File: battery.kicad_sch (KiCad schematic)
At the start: 38 parts

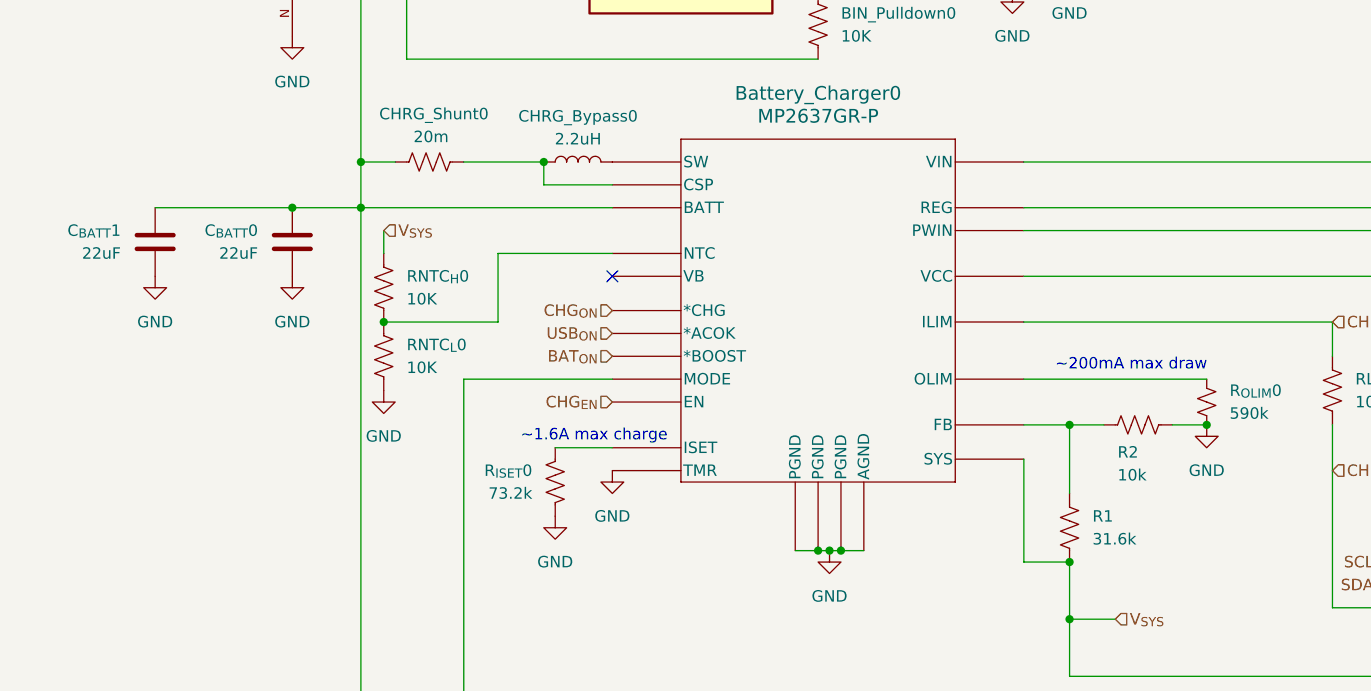
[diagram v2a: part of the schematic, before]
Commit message: Assign footprints
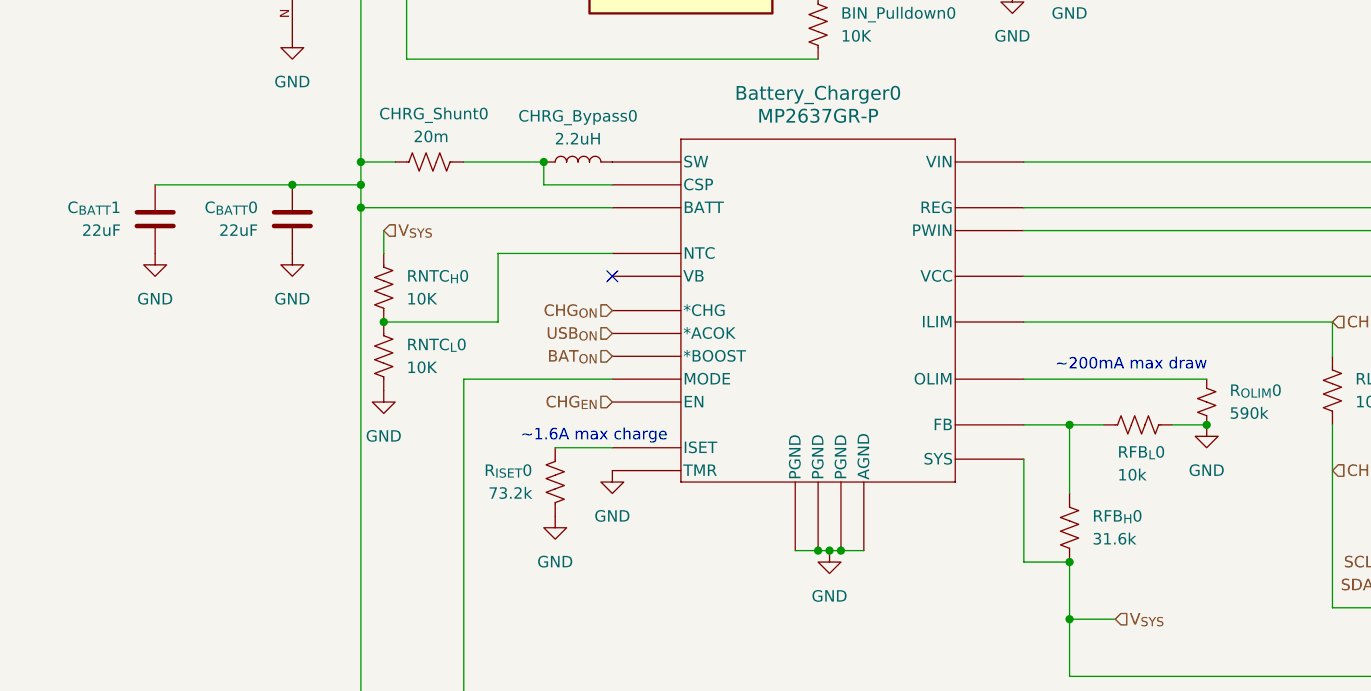
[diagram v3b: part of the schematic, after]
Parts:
- BAT0: footprint 1042:BAT_1042 -> BAT_1042
- BAT_Decouple0, CHRG_Decouple0, VDD_Decouple0: footprint (none) -> Capacitor_SMD:C_0402_1005Metric
- BAT_MIN0: footprint DMG2305UX-7:SOT91P240X110-3N_DMG2305UX-7 -> SOT91P240X110-3N_DMG2305UX-7
- BIN_Pulldown0, RLIM_{H}0, RNTC_{H}0, RNTC_{L}0, R_{ISET}0, R_{Pullup}0, R_{Store}0: footprint (none) -> Resistor_SMD:R_0402_1005Metric
- Battery_Monitor0: footprint BQ27427YZFR:IC_BQ27427YZFR -> IC_BQ27427YZFR
- CHRG_Bypass0: footprint (none) -> Inductor_SMD:L_1210_3225Metric
- CHRG_Shunt0, RREG_{H}0, R_{HIST}0: footprint (none) -> Resistor_SMD:R_0805_2012Metric
- C_{BATT}0, C_{BATT}1, C_{SYS}0, C_{SYS}1, C_{SYS}2, VBUS_Bypass0: footprint (none) -> Capacitor_SMD:C_1206_3216Metric
- RFB_{H}0: renamed from R1; footprint (none) -> Resistor_SMD:R_0402_1005Metric
- RFB_{L}0: renamed from R2; footprint (none) -> Resistor_SMD:R_0402_1005Metric
- RLIM_Decouple0: footprint (none) -> Capacitor_SMD:C_0201_0603Metric
- RLIM_{L}0: footprint MCP40D19T-104E_LT:SOT65P210X110-5N -> SOT65P210X110-5N
- RREG_{L}0, RWIN_{H}0, RWIN_{L}0, R_{Lower}0, R_{OLIM}0, R_{Upper}0: footprint (none) -> Resistor_SMD:R_0603_1608Metric
- STORE_EN0: footprint EG2208:SW_EG2208 -> SW_EG2208
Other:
- moved on the sheet: C_{BATT}0, C_{BATT}1

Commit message: Init right and left PCBs
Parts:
- renumbered BAT0 to BAT1, BAT_Decouple0 to BAT_Decouple1, BAT_EN0 to BAT_EN1, BAT_Fuse0 to BAT_Fuse1, BAT_MIN0 to BAT_MIN1, BIN_Pulldown0 to BIN_Pulldown1, Battery_Charger0 to Battery_Charger1, Battery_Monitor0 to Battery_Monitor1, CHRG_Bypass0 to CHRG_Bypass1, CHRG_Decouple0 to CHRG_Decouple1, CHRG_Shunt0 to CHRG_Shunt1, C_{BATT}0 to C_{BATT}2, C_{SYS}0 to C_{SYS}1, C_{SYS}1 to C_{SYS}2, C_{SYS}2 to C_{SYS}3, RFB_{H}0 to RFB_{H}1, RFB_{L}0 to RFB_{L}1, RLIM_Decouple0 to RLIM_Decouple1, RLIM_{H}0 to RLIM_{H}1, RLIM_{L}0 to RLIM_{L}1, RNTC_{H}0 to RNTC_{H}1, RNTC_{L}0 to RNTC_{L}1, RREG_{H}0 to RREG_{H}1, RREG_{L}0 to RREG_{L}1, RWIN_{H}0 to RWIN_{H}1, RWIN_{L}0 to RWIN_{L}1, R_{HIST}0 to R_{HIST}1, R_{ISET}0 to R_{ISET}1, R_{Lower}0 to R_{Lower}1, R_{OLIM}0 to R_{OLIM}1, R_{Pullup}0 to R_{Pullup}1, R_{Store}0 to R_{Store}1, R_{Upper}0 to R_{Upper}1, STORE_EN0 to STORE_EN1, VBAT_PASS0 to VBAT_PASS1, VBUS_Bypass0 to VBUS_Bypass1, VDD_Decouple0 to VDD_Decouple1

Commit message: Rename keyswitch diodes
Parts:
- renumbered BAT1 to BAT0, BAT_Decouple1 to BAT_Decouple0, BAT_EN1 to BAT_EN0, BAT_Fuse1 to BAT_Fuse0, BAT_MIN1 to BAT_MIN0, BIN_Pulldown1 to BIN_Pulldown0, Battery_Charger1 to Battery_Charger0, Battery_Monitor1 to Battery_Monitor0, CHRG_Bypass1 to CHRG_Bypass0, CHRG_Decouple1 to CHRG_Decouple0, CHRG_Shunt1 to CHRG_Shunt0, C_{BATT}2 to C_{BATT}0, C_{SYS}1 to C_{SYS}0, C_{SYS}2 to C_{SYS}1, C_{SYS}3 to C_{SYS}2, RFB_{H}1 to RFB_{H}0, RFB_{L}1 to RFB_{L}0, RLIM_Decouple1 to RLIM_Decouple0, RLIM_{H}1 to RLIM_{H}0, RLIM_{L}1 to RLIM_{L}0, RNTC_{H}1 to RNTC_{H}0, RNTC_{L}1 to RNTC_{L}0, RREG_{H}1 to RREG_{H}0, RREG_{L}1 to RREG_{L}0, RWIN_{H}1 to RWIN_{H}0, RWIN_{L}1 to RWIN_{L}0, R_{HIST}1 to R_{HIST}0, R_{ISET}1 to R_{ISET}0, R_{Lower}1 to R_{Lower}0, R_{OLIM}1 to R_{OLIM}0, R_{Pullup}1 to R_{Pullup}0, R_{Store}1 to R_{Store}0, R_{Upper}1 to R_{Upper}0, STORE_EN1 to STORE_EN0, VBAT_PASS1 to VBAT_PASS0, VBUS_Bypass1 to VBUS_Bypass0, VDD_Decouple1 to VDD_Decouple0
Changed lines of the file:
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@@
 		(dnp no)
 		(fields_autoplaced yes)
-		(property "Reference" "RREG_{H}1"
+		(property "Reference" "RREG_{H}0"
 			(at 217.17 77.4699 0)
 			(effects
@@
 		(dnp no)
 		(fields_autoplaced yes)
-		(property "Reference" "#PWR0109"
+		(property "Reference" "#PWR030"
 			(at 181.61 147.32 0)
 			(effects
@@
 		(dnp no)
 		(fields_autoplaced yes)
-		(property "Reference" "#PWR0116"
+		(property "Reference" "#PWR021"
 			(at 85.09 121.92 0)
 			(effects
@@
 		(on_board yes)
 		(dnp no)
-		(property "Reference" "R_{Lower}1"
+		(property "Reference" "R_{Lower}0"
 			(at 103.378 185.42 0)
 			(effects
@@
 		(on_board yes)
 		(dnp no)
-		(property "Reference" "BAT_MIN1"
+		(property "Reference" "BAT_MIN0"
 			(at 158.75 143.51 90)
 			(effects
@@
 		(dnp no)
 		(fields_autoplaced yes)
-		(property "Reference" "#PWR0108"
+		(property "Reference" "#PWR013"
 			(at 157.48 111.76 0)
 			(effects
@@
 		(dnp no)
 		(fields_autoplaced yes)
-		(property "Reference" "Battery_Monitor1"
+		(property "Reference" "Battery_Monitor0"
 			(at 99.06 26.67 0)
 			(effects
@@
 		(on_board yes)
 		(dnp no)
-		(property "Reference" "RNTC_{L}1"
+		(property "Reference" "RNTC_{L}0"
 			(at 68.58 96.5199 0)
 			(effects
@@
 		(dnp no)
 		(fields_autoplaced yes)
-		(property "Reference" "RWIN_{L}1"
+		(property "Reference" "RWIN_{L}0"
 			(at 234.95 86.3599 0)
 			(effects
@@
 		(on_board yes)
 		(dnp no)
-		(property "Reference" "C_{SYS}1"
+		(property "Reference" "C_{SYS}0"
 			(at 177.8 135.8899 0)
 			(effects
@@
 		(dnp no)
 		(fields_autoplaced yes)
-		(property "Reference" "VDD_Decouple1"
+		(property "Reference" "VDD_Decouple0"
 			(at 118.11 49.5299 0)
 			(effects
@@
 		(dnp no)
 		(fields_autoplaced yes)
-		(property "Reference" "#PWR0120"
+		(property "Reference" "#PWR024"
 			(at 232.41 97.79 0)
 			(effects
@@
 		(dnp no)
 		(fields_autoplaced yes)
-		(property "Reference" "BAT_EN1"
+		(property "Reference" "BAT_EN0"
 			(at 76.2 143.51 0)
 			(effects
@@
 		(dnp no)
 		(fields_autoplaced yes)
-		(property "Reference" "#PWR0124"
+		(property "Reference" "#PWR027"
 			(at 40.64 92.71 0)
 			(effects
@@
 		(dnp no)
 		(fields_autoplaced yes)
-		(property "Reference" "VBAT_PASS1"
+		(property "Reference" "VBAT_PASS0"
 			(at 137.16 161.29 0)
 			(effects
@@
 		(on_board yes)
 		(dnp no)
-		(property "Reference" "CHRG_Shunt1"
+		(property "Reference" "CHRG_Shunt0"
 			(at 65.532 70.866 90)
 			(effects
@@
 		(on_board yes)
 		(dnp no)
-		(property "Reference" "C_{SYS}2"
+		(property "Reference" "C_{SYS}1"
 			(at 190.5 135.8899 0)
 			(effects
@@
 		(dnp no)
 		(fields_autoplaced yes)
-		(property "Reference" "RWIN_{H}1"
+		(property "Reference" "RWIN_{H}0"
 			(at 234.95 78.7399 0)
 			(effects
@@
 		(dnp no)
 		(fields_autoplaced yes)
-		(property "Reference" "#PWR0107"
+		(property "Reference" "#PWR018"
 			(at 135.89 63.5 0)
 			(effects
@@
 		(dnp no)
 		(fields_autoplaced yes)
-		(property "Reference" "CHRG_Decouple1"
+		(property "Reference" "CHRG_Decouple0"
 			(at 194.31 91.4399 0)
 			(effects
@@
 		(dnp no)
 		(fields_autoplaced yes)
-		(property "Reference" "#PWR0119"
+		(property "Reference" "#PWR012"
 			(at 214.63 100.33 0)
 			(effects
@@
 		(dnp no)
 		(fields_autoplaced yes)
-		(property "Reference" "Battery_Charger1"
+		(property "Reference" "Battery_Charger0"
 			(at 114.3 68.58 0)
 			(effects
@@
 		(dnp no)
 		(fields_autoplaced yes)
-		(property "Reference" "#PWR0121"
+		(property "Reference" "#PWR023"
 			(at 217.17 132.08 0)
 			(effects
@@
 		(on_board yes)
 		(dnp no)
-		(property "Reference" "#PWR0115"
+		(property "Reference" "#PWR025"
 			(at 115.57 125.73 0)
 			(effects
@@
 		(on_board yes)
 		(dnp no)
-		(property "Reference" "RNTC_{H}1"
+		(property "Reference" "RNTC_{H}0"
 			(at 68.58 88.8999 0)
 			(effects
@@
 		(dnp no)
 		(fields_autoplaced yes)
-		(property "Reference" "#PWR0110"
+		(property "Reference" "#PWR010"
 			(at 190.5 102.87 0)
 			(effects
@@
 		(on_board yes)
 		(dnp no)
-		(property "Reference" "RFB_{H}1"
+		(property "Reference" "RFB_{H}0"
 			(at 144.78 115.5699 0)
 			(effects
@@
 		(dnp no)
 		(fields_autoplaced yes)
-		(property "Reference" "#PWR0112"
+		(property "Reference" "#PWR031"
 			(at 194.31 147.32 0)
 			(effects
@@
 		(dnp no)
 		(fields_autoplaced yes)
-		(property "Reference" "#PWR0123"
+		(property "Reference" "#PWR016"
 			(at 55.88 68.58 0)
 			(effects
@@
 		(on_board yes)
 		(dnp no)
-		(property "Reference" "C_{BATT}2"
+		(property "Reference" "C_{BATT}0"
 			(at 52.07 81.2799 0)
 			(effects
@@
 		(dnp no)
 		(fields_autoplaced yes)
-		(property "Reference" "#PWR0113"
+		(property "Reference" "#PWR019"
 			(at 156.21 181.61 0)
 			(effects
@@
 		(dnp no)
 		(fields_autoplaced yes)
-		(property "Reference" "#PWR0111"
+		(property "Reference" "#PWR028"
 			(at 208.28 147.32 0)
 			(effects
@@
 		(on_board yes)
 		(dnp no)
-		(property "Reference" "R_{Upper}1"
+		(property "Reference" "R_{Upper}0"
 			(at 85.344 177.8 0)
 			(effects
@@
 		(dnp no)
 		(fields_autoplaced yes)
-		(property "Reference" "STORE_EN1"
+		(property "Reference" "STORE_EN0"
 			(at 81.28 157.48 0)
 			(effects
@@
 		(on_board yes)
 		(dnp no)
-		(property "Reference" "R_{Pullup}1"
+		(property "Reference" "R_{Pullup}0"
 			(at 136.144 152.4 0)
 			(effects
@@
 		(dnp no)
 		(fields_autoplaced yes)
-		(property "Reference" "CHRG_Bypass1"
+		(property "Reference" "CHRG_Bypass0"
 			(at 87.63 71.12 90)
 			(effects
@@
 		(dnp no)
 		(fields_autoplaced yes)
-		(property "Reference" "#PWR0122"
+		(property "Reference" "#PWR029"
 			(at 250.19 90.17 0)
 			(effects
@@
 		(dnp no)
 		(fields_autoplaced yes)
-		(property "Reference" "#PWR0125"
+		(property "Reference" "#PWR022"
 			(at 55.88 92.71 0)
 			(effects
@@
 		(dnp no)
 		(fields_autoplaced yes)
-		(property "Reference" "VBUS_Bypass1"
+		(property "Reference" "VBUS_Bypass0"
 			(at 254 78.7399 0)
 			(effects
@@
 		(dnp no)
 		(fields_autoplaced yes)
-		(property "Reference" "#PWR0117"
+		(property "Reference" "#PWR026"
 			(at 66.04 107.95 0)
 			(effects
@@
 		(dnp no)
 		(fields_autoplaced yes)
-		(property "Reference" "R_{HIST}1"
+		(property "Reference" "R_{HIST}0"
 			(at 167.64 162.5599 0)
 			(effects
@@
 		(on_board yes)
 		(dnp no)
-		(property "Reference" "R_{ISET}1"
+		(property "Reference" "R_{ISET}0"
 			(at 82.55 110.4899 0)
 			(effects
@@
 		(dnp no)
 		(fields_autoplaced yes)
-		(property "Reference" "RLIM_Decouple1"
+		(property "Reference" "RLIM_Decouple0"
 			(at 219.71 121.9262 0)
 			(effects
@@
 		(on_board yes)
 		(dnp no)
-		(property "Reference" "RLIM_{H}1"
+		(property "Reference" "RLIM_{H}0"
 			(at 173.99 100.3299 0)
 			(effects
@@
 		(dnp no)
 		(fields_autoplaced yes)
-		(property "Reference" "BIN_Pulldown1"
+		(property "Reference" "BIN_Pulldown0"
 			(at 116.84 59.6899 0)
 			(effects
@@
 		(on_board yes)
 		(dnp no)
-		(property "Reference" "R_{Store}1"
+		(property "Reference" "R_{Store}0"
 			(at 97.282 177.8 0)
 			(effects
@@
 		(on_board yes)
 		(dnp no)
-		(property "Reference" "RFB_{L}1"
+		(property "Reference" "RFB_{L}0"
 			(at 147.574 108.458 90)
 			(effects
@@
 		(dnp no)
 		(fields_autoplaced yes)
-		(property "Reference" "R_{OLIM}1"
+		(property "Reference" "R_{OLIM}0"
 			(at 160.02 101.5999 0)
 			(effects
@@
 		(dnp no)
 		(fields_autoplaced yes)
-		(property "Reference" "BAT_Decouple1"
+		(property "Reference" "BAT_Decouple0"
 			(at 140.97 49.5299 0)
 			(effects
@@
 		(dnp no)
 		(fields_autoplaced yes)
-		(property "Reference" "#PWR0118"
+		(property "Reference" "#PWR09"
 			(at 91.44 116.84 0)
 			(effects
@@
 		(dnp no)
 		(fields_autoplaced yes)
-		(property "Reference" "#PWR0106"
+		(property "Reference" "#PWR020"
 			(at 142.24 60.96 0)
 			(effects
@@
 		(on_board yes)
 		(dnp no)
-		(property "Reference" "BAT_Fuse1"
+		(property "Reference" "BAT_Fuse0"
 			(at 36.322 40.132 90)
 			(effects
@@
 		(on_board yes)
 		(dnp no)
-		(property "Reference" "RLIM_{L}1"
+		(property "Reference" "RLIM_{L}0"
 			(at 197.8279 110.49 0)
 			(effects
@@
 		(on_board yes)
 		(dnp no)
-		(property "Reference" "C_{SYS}3"
+		(property "Reference" "C_{SYS}2"
 			(at 204.47 135.8899 0)
 			(effects
@@
 		(on_board yes)
 		(dnp no)
-		(property "Reference" "BAT1"
+		(property "Reference" "BAT0"
 			(at 46.736 53.34 90)
 			(effects
@@
 		(dnp no)
 		(fields_autoplaced yes)
-		(property "Reference" "#PWR0114"
+		(property "Reference" "#PWR017"
 			(at 111.76 195.58 0)
 			(effects
@@
 		(on_board yes)
 		(dnp no)
-		(property "Reference" "RREG_{L}1"
+		(property "Reference" "RREG_{L}0"
 			(at 217.17 88.8999 0)
 			(effects

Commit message: Make battery holder thru-hole
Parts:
- BAT0: value 1042 -> 1043; footprint BAT_1042 -> BAT_1043
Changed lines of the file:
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@@
 			)
 		)
-		(property "Value" "1042"
+		(property "Value" "1043"
 			(at 46.736 55.88 90)
 			(effects
@@
 			)
 		)
-		(property "Footprint" "BAT_1042"
+		(property "Footprint" "BAT_1043"
 			(at 55.88 54.61 0)
 			(effects
